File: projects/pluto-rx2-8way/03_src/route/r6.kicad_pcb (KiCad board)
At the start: 4 copper layers, 50 x 71 mm, 68 parts

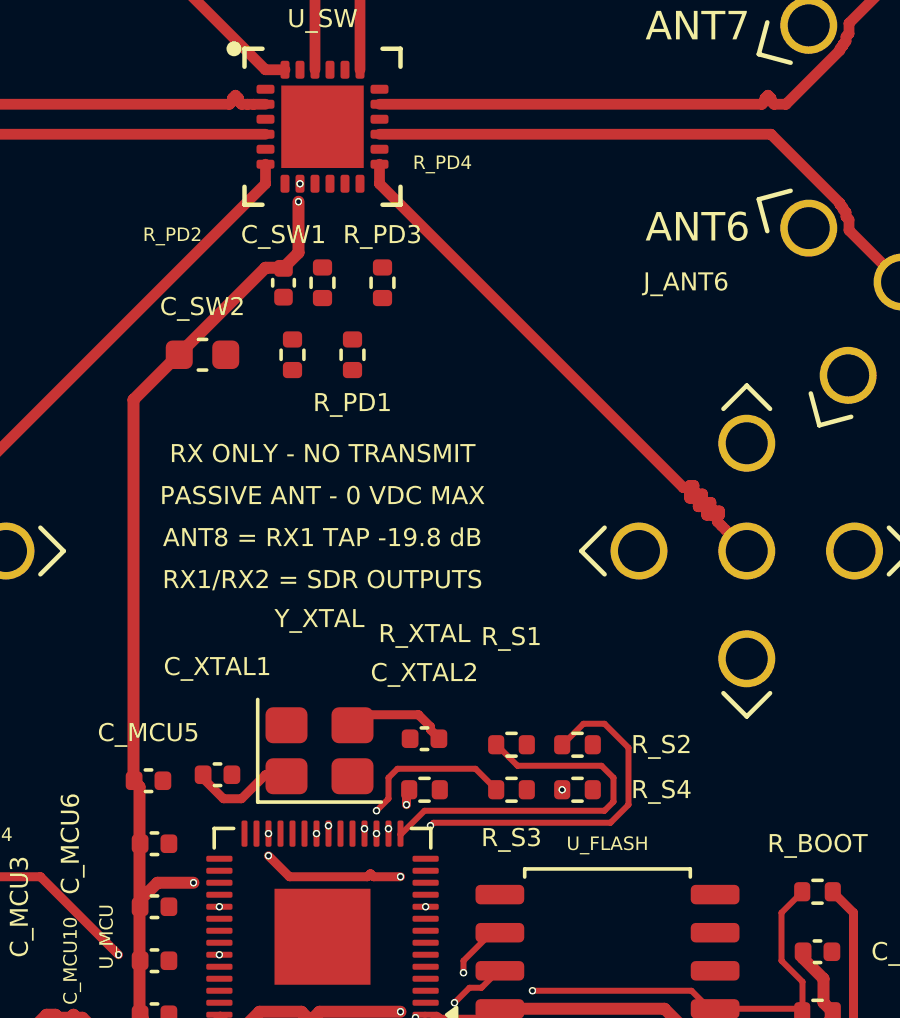
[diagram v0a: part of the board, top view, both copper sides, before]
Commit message: the RF-fan keepout contradicted the comment directly above it, and four nets paid 0.000 mm of copper for it
prep.keepouts.rects carried ONE rect {21, 21, 71, 65} on User.3 for the
ctrl/qspi/sig waves. The comment above it says those buses "must descend
through the 225-315 degree escape sector on L3". The rect closed that sector.

WHAT IT COST, MEASURED. The rect CONTAINED the endpoints of four nets.
SW_V1..SW_V4 leave U_SW's SOUTH LEAD ROW (pads 9-12, y 47.900,
x 45.75..47.25) onto R_PD1-4.1 (y 50.690 / 53.090) — all eight pads INSIDE
the keepout — while their far ends R_S1-4.2 (y 66.6 / 68.1) sit outside it.
The four nets carried 0.000 mm of track copper anywhere on the board and
were 8 of the 28 unconnected. KRT's own docstring names this exact failure
(obstacle_map.add_user_keepout_obstacles): "a zone drawn over a routed net's
pad can make that net unroutable -- zones are meant for open board area, not
over pads." And the zone blocks ALL COPPER LAYERS, so the L3 descent the
comment prescribes was blocked too — the keepout layer tags which WAVE sees
a zone, never which copper layer it frees.

THE WEDGE IS EMPTY BY CONSTRUCTION. The ten jacks sit at 15/45/75/105/135/
165/195/225 and 315/345 degrees; 240..300 HAS NO JACK, which is why the
escape sector was specified there. Measured on the promoted chain: the only
RF copper south of y=52 is ANT4 running to J_ANT4 at 225 deg and ANT5 to
J_ANT5 at 315 deg, and the channel between them opens from 1.5 mm at y=47
to 32 mm at y=61.

FITTED TO MEASURED COPPER, NOT TO A MODEL. A linear fit to the ANT4/ANT5
diagonals was tried first and was WRONG BY 0.65 mm — the trombone meanders
push ANT4 out to x=42.5 and the corridor grazed it at 0.0000 mm. Refitted at
0.60 mm off the measured centrelines over each band: all 8 SW pads free by
BOUNDING BOX (not centre), 0 ctrl/qspi pads still covered, and the 373.44
mm2 opened comes no closer than 0.5000 mm to any RF centreline = 0.320 mm to
arm copper at the 0.36 mm width, against the 0.2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
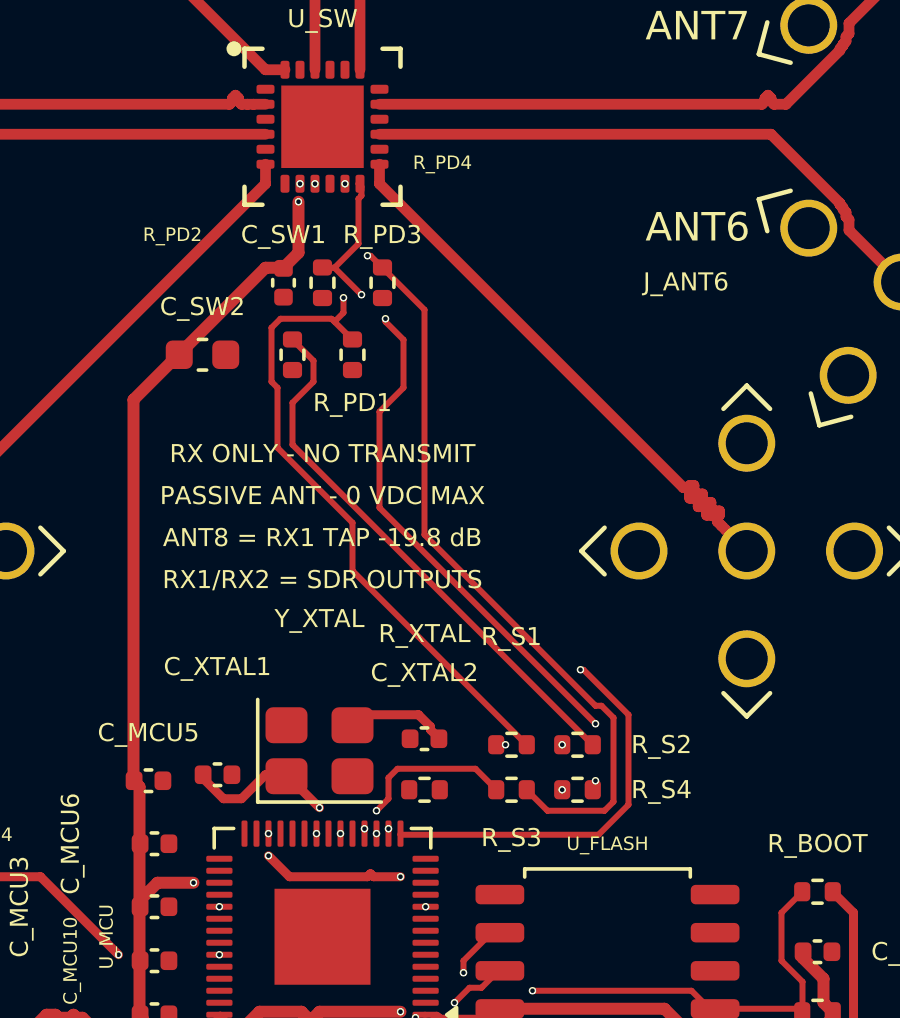
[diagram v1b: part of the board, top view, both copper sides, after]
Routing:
- net SW_V3: track 0.00 -> 27.8 mm, vias 0 -> 2
- net SW_V1: track 0.00 -> 25.6 mm, vias 0 -> 2
- net SW_V4: track 0.00 -> 25.4 mm, vias 0 -> 4
- net SW_V2: track 0.00 -> 18.2 mm
- net XOUT: track 7.21 -> 0.00 mm, vias 2 -> 0
- net SEL_V1: track 12.7 -> 17.1 mm, vias 0 -> 2
- net SEL_V2: track 13.1 -> 8.80 mm
- net XIN: track 3.59 -> 6.34 mm, vias 0 -> 2

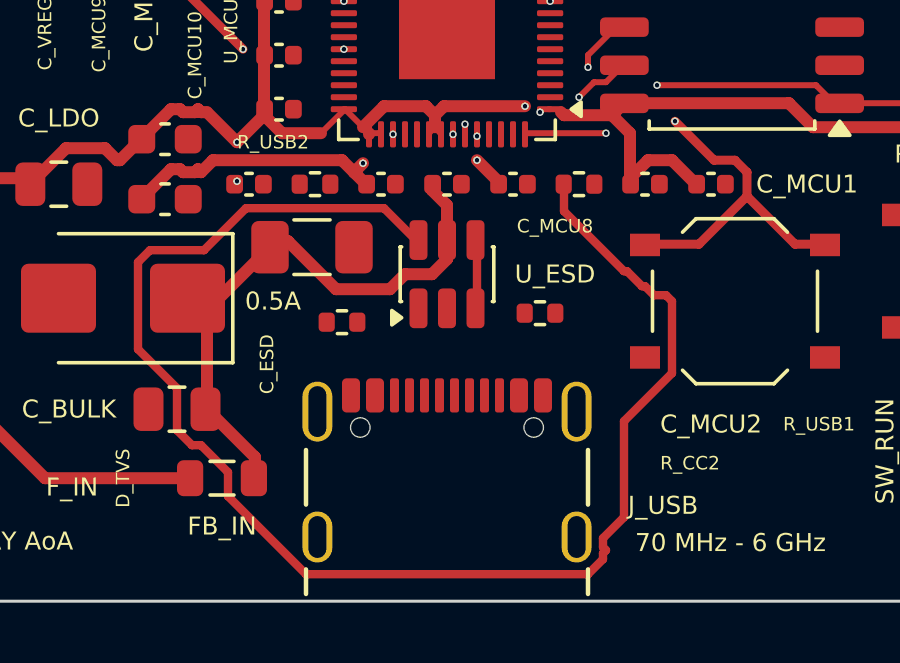
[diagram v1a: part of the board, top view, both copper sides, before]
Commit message: J_USB's 0.650 mm alignment pegs were read as M3 mounting holes and fenced at the M3 radius — 2.5 mm of over-reach that buried all 16 of its pads
prep.keepouts.mounting_holes has NO refdes filter by default, so
route_and_stitch_generic stamps a 2r x 2r rect around EVERY NPTH PAD ON THE
BOARD. J_USB is a through-hole-anchored USB-C receptacle whose vendor land
carries two 0.650 mm ALIGNMENT PEGS at (43.110, 86.210) and (48.890,
86.210). They are NPTH, so they were fenced at radius 3.0 — the M3 head
radius — where the nearest J_USB copper edge is 0.5000 mm away. MEASURED:
the two 6.0 x 6.0 mm rects union to x 40.110..51.890 / y 83.210..89.210 and
cover ALL 16 J_USB SMD pads at y 85.140, i.e. 2.5 mm of over-reach took out
USB_DM, USB_DP, VBUS, USB_CC1 and USB_CC2 — 10 of the 28 unconnected.

THE NAMED FIX WAS ARITHMETICALLY WRONG AND WOULD HAVE RE-CREATED THIS BUG AT
ONE FIFTH THE SCALE, where it would have been far harder to see. The
prescribed `npth_pads` margin of 0.25 gives r = drill/2 + margin = 0.325 +
0.25 = 0.575 mm, against a closest pad edge of 0.5000 mm from the peg
centre. Measured against the actual pads:
    margin 0.25 -> r 0.575 -> COVERS 8 PADS (A1 GND, A4/A9 VBUS, ...)
    margin 0.20 -> r 0.525 -> COVERS 8 PADS
    margin 0.15 -> r 0.475 -> 0 pads covered, 0.025 mm of slack
0.15 is not a tuned number either: it is floorplan.yaml's own
`hole_clearance: 0.15` (line 614), the DRC quantity this fence exists to
satisfy. VERIFIED AFTER THE CHANGE: 0 J_USB SMD pads inside any keepout.

THE CAVEAT WAS REAL BUT IT RESOLVED IN OUR FAVOUR, AND BY MEASUREMENT.
Unlike the User.3 work, these rects are stamped on BOTH layers in
prep.keepouts.layers, so the rf wave DOES read them and the User.2 SET
genuinely changes: 2 rects of 6.0 x 6.0 removed, 6 added. But four of the
six are the H1..H4 npth_pads rects at 3.5 x 3.5, which sit STRICTLY INSIDE
the existing 6 x 6 mounting_holes rects and are therefore subsumed — so the
only functional change is confined to the band y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
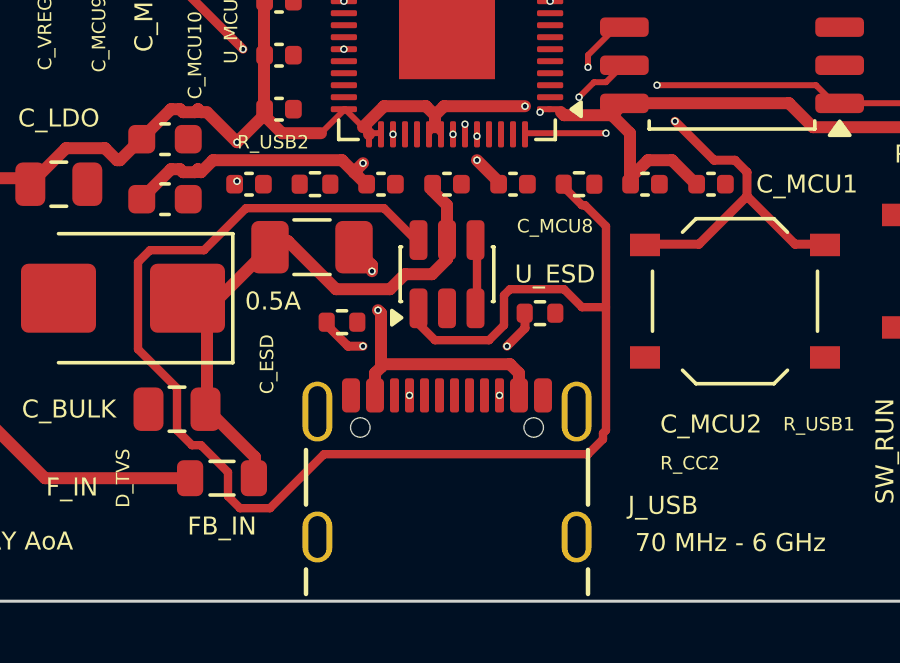
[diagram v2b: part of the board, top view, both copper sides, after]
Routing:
- net VBUS: track 0.00 -> 10.9 mm, vias 0 -> 2
- net USB_CC1: track 0.00 -> 3.85 mm, vias 0 -> 2
- net USB_CC2: track 0.00 -> 3.03 mm, vias 0 -> 2
- net USB_DP: track 49.0 -> 51.2 mm
